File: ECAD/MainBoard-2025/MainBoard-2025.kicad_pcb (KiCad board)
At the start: 2 copper layers, 56 x 151 mm, 144 parts, among them J1 XT60, J12 Conn_01x04, J15 Conn_01x02, J16 XT30, J18 Conn_01x02, J2 Conn_01x04, J20 BAU, J21 BAU, J22 Conn_01x04, J23 Conn_01x02, J26 BAU, J28 Conn_01x02, J4 Conn_01x02, J6 Conn_01x06, J7 XT30, J8 Conn_01x02, J9 Conn_01x02, K2 FINDER-36.11, U2 R-78B3.3-2.0, U3 R-78B12-2.0, U4 R-78B5.0-2.0, U5 Teensy4.1

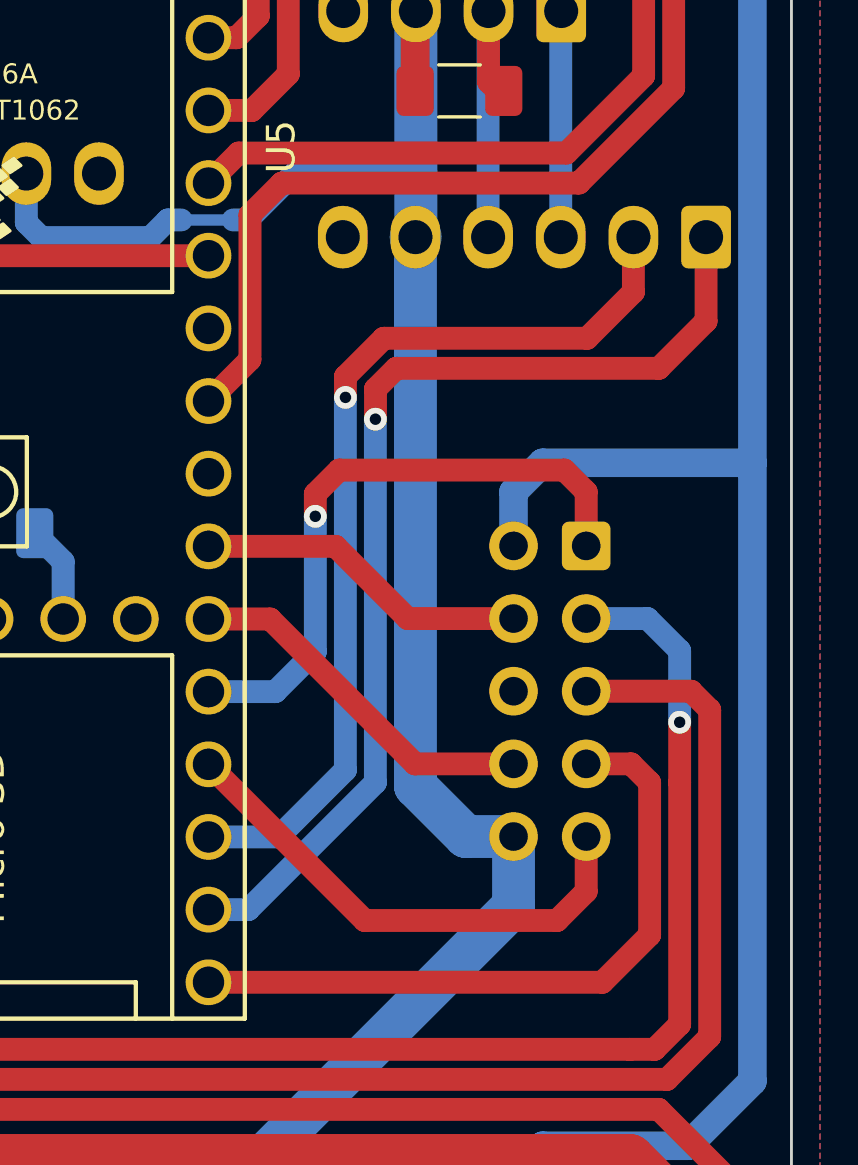
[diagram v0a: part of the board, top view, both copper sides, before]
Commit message: WIP - comatibility 3.x 4.x
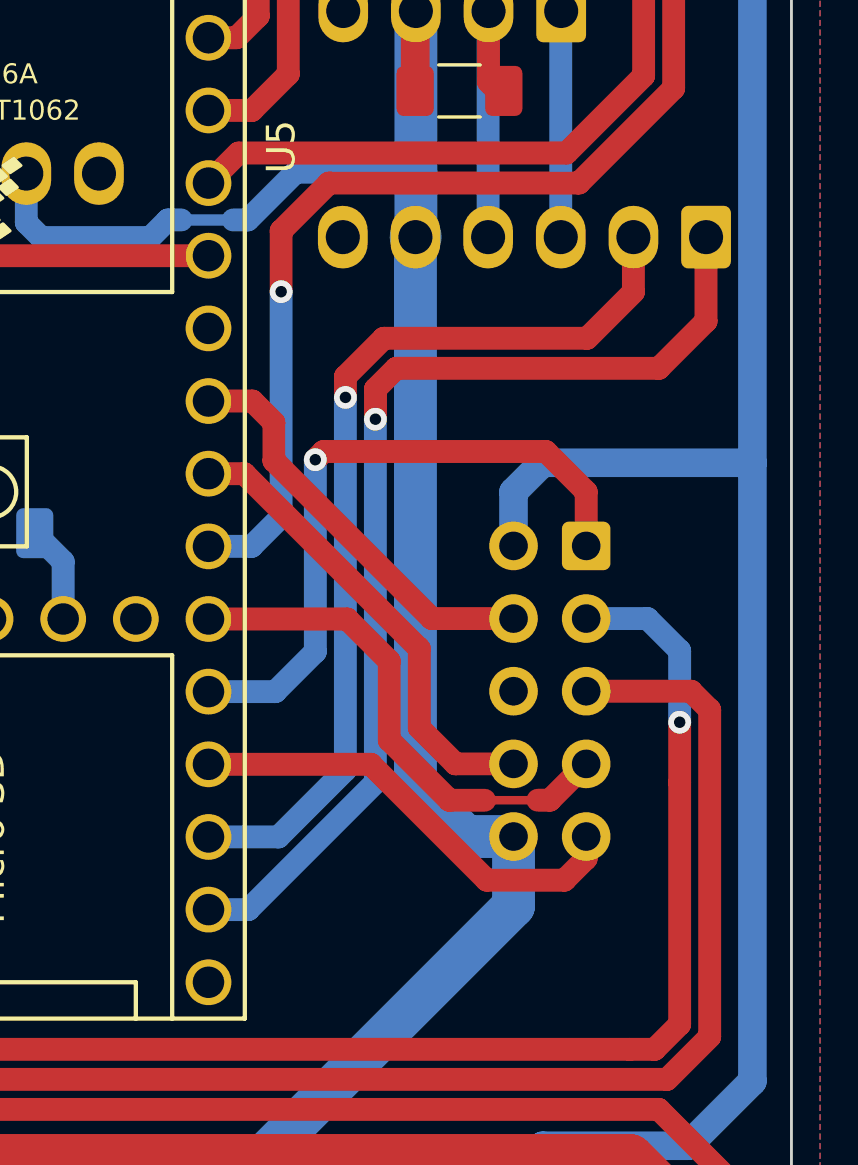
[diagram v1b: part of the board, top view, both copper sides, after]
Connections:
- IHM-IO1 pad 5: Detection -> Tirette-2
- IHM-IO1 pad 7: IHM_3 -> Init-2
- IHM-IO1 pad 9: IHM_4 -> Detection
- U5 pad 24: Detection -> Tirette-2
- U5 pad 25: IHM_3 -> unconnected-(U5-33_MCLK2-Pad25)
- U5 pad 28: IHM_4 -> Detection
- U5 pad 30: Analog0 -> Init-2
- U5 pad 31: Analog1 -> C_Act1-6
- U5 pad 32: unconnected-(U5-40_A16-Pad32) -> Analog0
- U5 pad 33: C_Act1-6 -> Analog1
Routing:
- net Tirette-2: track 0.00 -> 50.8 mm
- net Detection: track 50.8 -> 16.0 mm
- net IHM_3: track 23.9 -> 0.00 mm
- net Init-2: track 0.00 -> 18.0 mm
- net IHM_4: track 17.8 -> 0.00 mm
- net C_Act1-6: track 45.0 -> 50.0 mm, vias 0 -> 1
- net Analog0: track 12.8 -> 16.5 mm
- net Analog1: track 11.7 -> 14.6 mm
- net NEO_PIXEL: track 21.9 -> 23.1 mm

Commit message: Mise en concordance du buzzer avec carte Pami
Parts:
- removed BZ1: Buzzer, Buzzer_Beeper:Buzzer_15x7.5RM7.6
- added BZ2: Buzzer, Buzzer_Beeper:Buzzer_12x9.5RM7.6, F.Cu at (79.6, 99.0)
- moved G*** 188.9 mm to (-37.9, 192.8)
- moved G*** 188.9 mm to (35.5, 116.3)
- moved G*** 188.9 mm to (2.24, 172.7)
- moved G*** 188.9 mm to (15.2, 137.9)
- moved G*** 188.9 mm to (-47.5, 194.7)
- moved G*** 188.9 mm to (44.9, 116.3)
- moved G*** 188.9 mm to (17.2, 109.0)
- moved G*** 188.9 mm to (-21.2, 199.9)
- moved G*** 188.9 mm to (-16.1, 203.7)
- moved G*** 188.9 mm to (43.6, 193.8)
- moved G*** 188.9 mm to (20.6, 190.1)
- moved G*** 188.9 mm to (-47.8, 179.4)
- moved G*** 188.9 mm to (7.82, 137.9)
- moved kibuzzard-64933096 188.9 mm to (25.3, 191.3)
- moved kibuzzard-6493EE56 188.9 mm to (-30.4, 142.5)
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
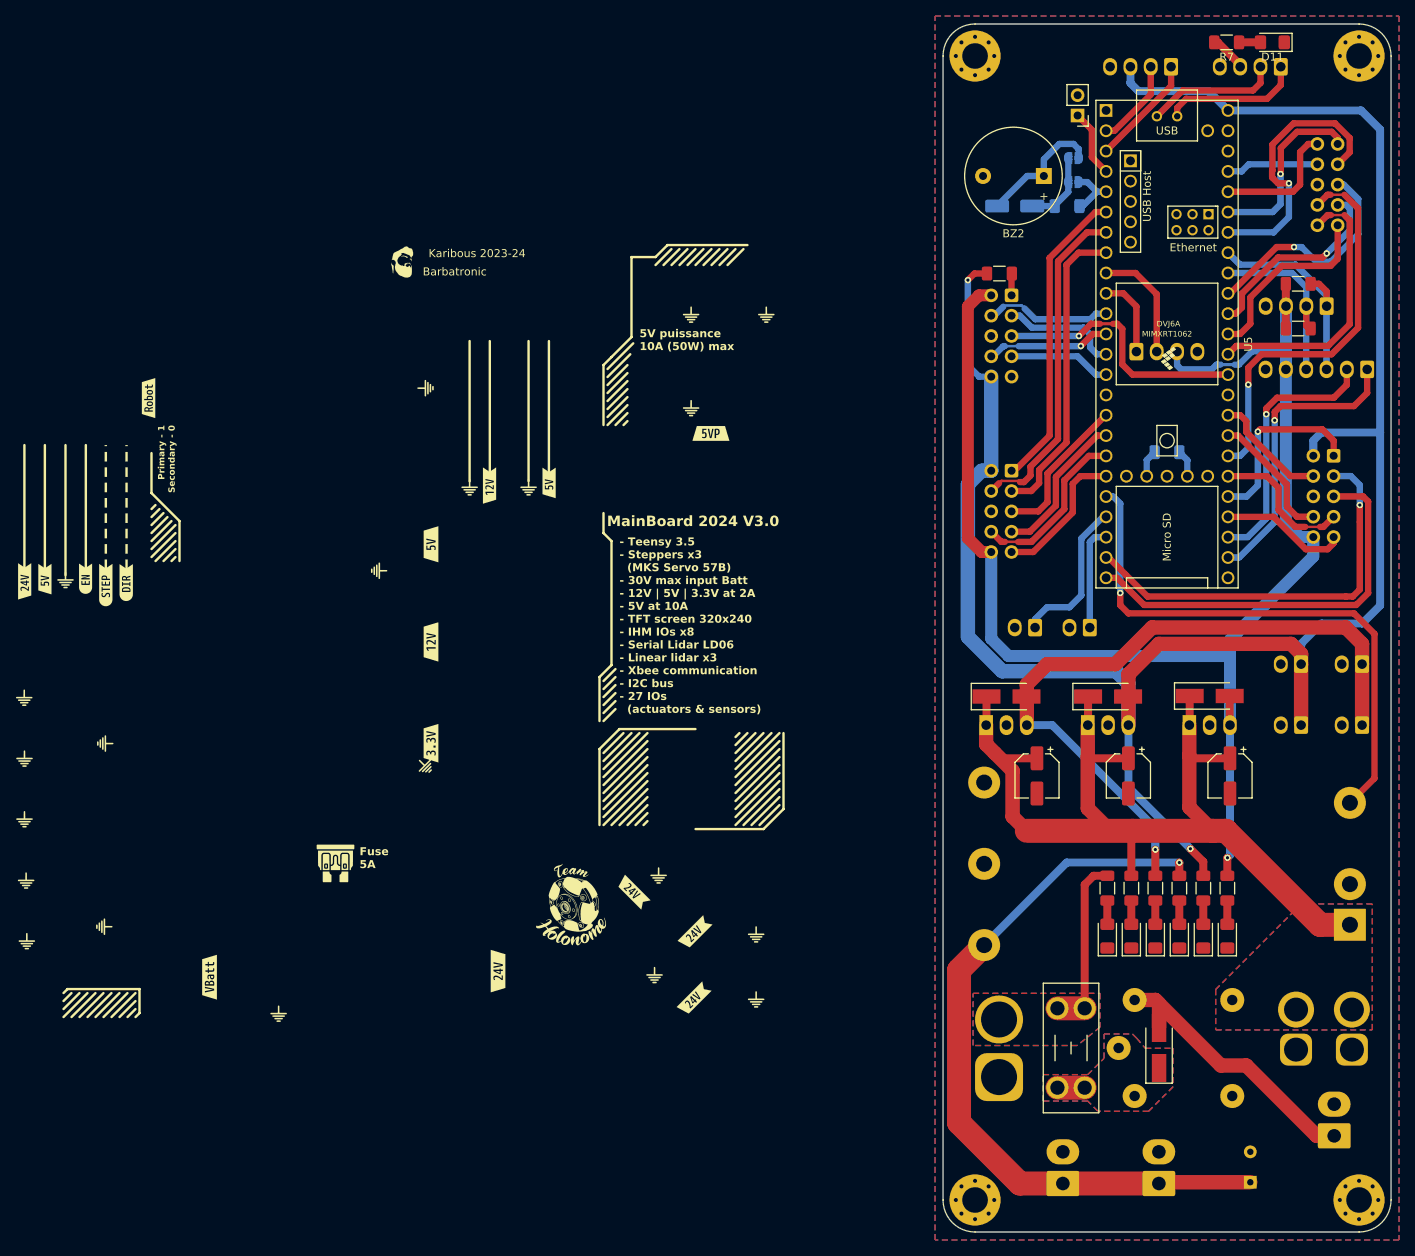
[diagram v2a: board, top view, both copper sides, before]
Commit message: Ne Silkscreen - Optimize for 3.5 and 4.1
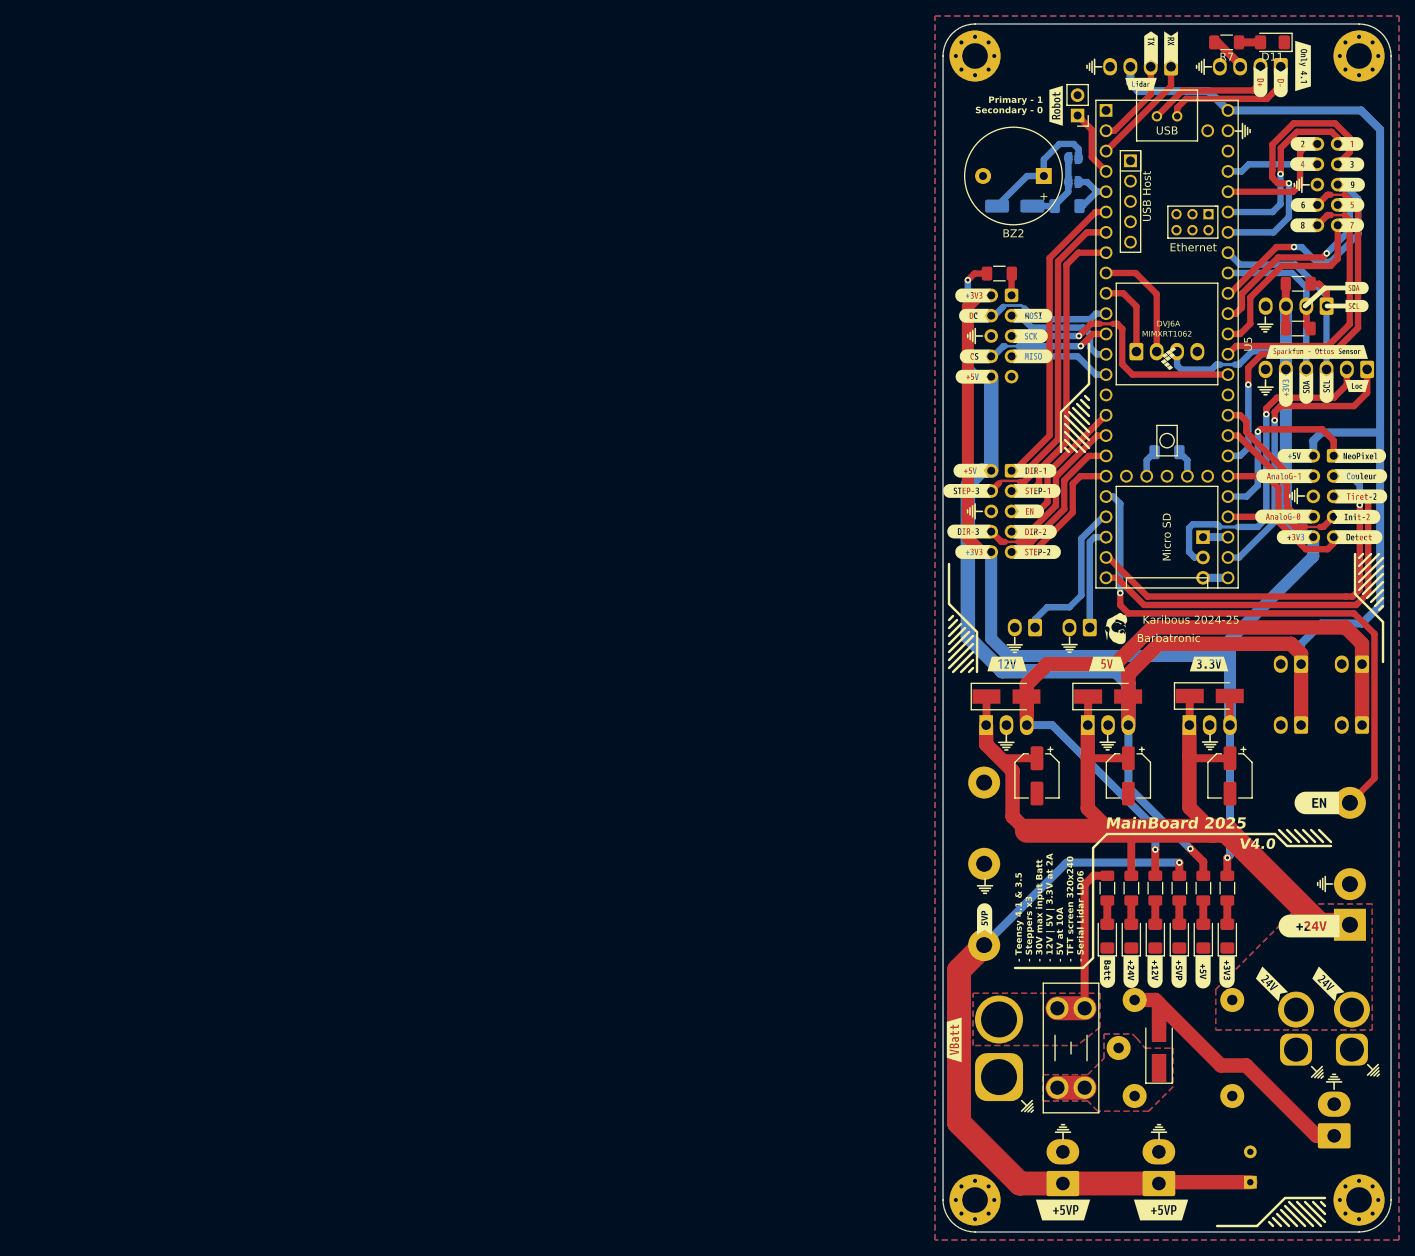
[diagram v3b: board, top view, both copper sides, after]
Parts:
- removed the G*** at (43.6, 201.9)
- removed the G*** at (-3.49, 148.3)
- removed the G*** at (-37.9, 192.8)
- removed the G*** at (35.5, 116.3)
- removed the G*** at (2.24, 172.7)
- removed the G*** at (-42.7, 149.5)
- removed the G*** at (15.2, 137.9)
- removed the G*** at (-47.5, 194.7)
- removed the G*** at (35.5, 128.0)
- removed the G*** at (-47.6, 187.1)
- removed the G*** at (-47.8, 164.2)
- removed the G*** at (31.4, 186.5)
- removed the G*** at (-47.8, 171.8)
- removed the G*** at (44.9, 116.3)
- removed the G*** at (30.9, 198.9)
- removed the G*** at (2.32, 125.5)
- removed the G*** at (-37.7, 169.9)
- removed the G*** at (-30.9, 118.7)
- removed the G*** at (15.2, 115.6)
- removed the G*** at (17.2, 109.0)
- removed the G*** at (7.75, 115.6)
- removed the G*** at (-21.2, 199.9)
- removed the G*** at (-16.1, 203.7)
- removed the G*** at (-42.7, 114.8)
- removed the G*** at (-31.6, 154.7)
- removed the G*** at (30.9, 199.7)
- removed the G*** at (18.7, 181.1)
- removed the G*** at (38.0, 125.2)
- removed the G*** at (43.6, 193.8)
- removed the G*** at (-0.64, 109.7)
- removed the G*** at (-47.8, 179.4)
- removed the G*** at (7.82, 137.9)
- removed the G*** at (-8.94, 184.9)
- removed kibuzzard-64932E55: G***, kibuzzard-64932E55
- removed kibuzzard-64932EB2 (x2): G***, kibuzzard-64932EB2
- removed kibuzzard-64932F6F (x2): G***, kibuzzard-64932F6F
- removed kibuzzard-64933096: G***, kibuzzard-64933096
- removed kibuzzard-64933122: G***, kibuzzard-64933122
- removed kibuzzard-64933136: G***, kibuzzard-64933136
- removed kibuzzard-64933140: G***, kibuzzard-64933140
- removed kibuzzard-6493EE40: G***, kibuzzard-6493EE40
- removed kibuzzard-6493EE50: G***, kibuzzard-6493EE50
- removed kibuzzard-6493EE56: G***, kibuzzard-6493EE56
- removed kibuzzard-6493EE83: G***, kibuzzard-6493EE83
- removed kibuzzard-6493EEE0: G***, kibuzzard-6493EEE0
- removed kibuzzard-6493EEF0: G***, kibuzzard-6493EEF0
- removed kibuzzard-6493EF75: G***, kibuzzard-6493EF75
- removed kibuzzard-6493EFD0: G***, kibuzzard-6493EFD0
- removed kibuzzard-6493EFE7: G***, kibuzzard-6493EFE7
- removed kibuzzard-6493EFEC: G***, kibuzzard-6493EFEC
- removed kibuzzard-6493F0C8: G***, kibuzzard-6493F0C8
- removed kibuzzard-6493F174: G***, kibuzzard-6493F174
- removed kibuzzard-6493F18B: G***, kibuzzard-6493F18B
- removed kibuzzard-6493F190: G***, kibuzzard-6493F190
- removed kibuzzard-649443C2: G***, kibuzzard-649443C2
- removed kibuzzard-649443F6: G***, kibuzzard-649443F6
- removed kibuzzard-64944CDF: G***, kibuzzard-64944CDF
- removed kibuzzard-64944CEA: G***, kibuzzard-64944CEA
- removed kibuzzard-64944CF9: G***, kibuzzard-64944CF9
- removed kibuzzard-64944D19 (x2): G***, kibuzzard-64944D19
- removed the kibuzzard-64944D37 at (35.9, 201.9)
- removed the kibuzzard-64944D37 at (28.3, 188.5)
- removed the kibuzzard-64944D37 at (-47.8, 149.7)
- removed the kibuzzard-64944D37 at (36.0, 193.6)
- removed kibuzzard-64944DAA: G***, kibuzzard-64944DAA
- added G***: LOGO, LOGO, F.Cu at (76.0, 157.6)
- added G***: LOGO, LOGO, F.Cu at (74.9, 169.8)
- added G***: LOGO, LOGO, F.Cu at (82.0, 218.5)
- added G***: LOGO, LOGO, F.Cu at (99.6, 85.4)
- added G***: LOGO, LOGO, F.Cu at (71.0, 119.0)
- added G***: LOGO, LOGO, F.Cu at (82.8, 157.6)
- added G***: LOGO, LOGO, F.Cu at (85.9, 85.4)
- added G***: LOGO, LOGO, F.Cu at (114.8, 187.5)
- added G***: LOGO, LOGO, F.Cu at (111.8, 100.1)
- added G***: LOGO, LOGO, F.Cu at (87.6, 169.8)
- added G***: LOGO, LOGO, F.Cu at (120.8, 210.8)
- added G***: LOGO, LOGO, F.Cu at (113.8, 211.0)
- added G***: LOGO, LOGO, F.Cu at (77.5, 215.2)
- added G***: LOGO, LOGO, F.Cu at (72.2, 187.8)
- added G***: LOGO, LOGO, F.Cu at (94.0, 218.5)
- added G***: LOGO, LOGO, F.Cu at (107.3, 117.6)
- added G***: LOGO, LOGO, B.Cu at (82.5, 85.2)
- added G***: LOGO, LOGO, B.Cu at (81.5, 88.9)
- added G***: LOGO, LOGO, B.Cu at (114.8, 187.5)
- added G***: LOGO, LOGO, B.Cu at (75.4, 185.0)
- added G***: LOGO, LOGO, B.Cu at (83.0, 208.0)
- added G***: LOGO, LOGO, F.Cu at (111.2, 139.0)
- added G***: LOGO, LOGO, B.Cu at (120.8, 210.8)
- added G***: LOGO, LOGO, B.Cu at (115.9, 212.2)
- added G***: LOGO, LOGO, B.Cu at (107.4, 160.0)
- added G***: LOGO, LOGO, B.Cu at (85.9, 85.4)
- added G***: LOGO, LOGO, B.Cu at (82.0, 218.5)
- added G***: LOGO, LOGO, B.Cu at (95.0, 125.5)
- added G***: LOGO, LOGO, B.Cu at (113.8, 211.0)
- added G***: LOGO, LOGO, B.Cu at (77.5, 215.2)
- added G***: LOGO, LOGO, B.Cu at (115.0, 160.0)
- added G***: LOGO, LOGO, B.Cu at (107.4, 167.6)
- added G***: LOGO, LOGO, F.Cu at (104.5, 93.4)
- added G***: LOGO, LOGO, B.Cu at (94.0, 218.5)
- added G***: LOGO, LOGO, B.Cu at (108.7, 214.2)
- added G***: LOGO, LOGO, B.Cu at (115.0, 167.6)
- added G***: LOGO, LOGO, B.Cu at (118.2, 152.8)
- added G***: LOGO, LOGO, F.Cu at (107.3, 125.4)
- added G***: LOGO, LOGO, F.Cu at (115.9, 212.2)
- added G***: LOGO, LOGO, F.Cu at (71.0, 140.9)
- added G***: LOGO, LOGO, F.Cu at (88.6, 155.6)
- added G***: LOGO, LOGO, F.Cu at (100.4, 169.8)
- added J3: Conn_01x03, Connector_PinHeader_2.54mm:PinHeader_1x03_P2.54mm_Vertical, B.Cu at (99.5, 144.1)
- added kibuzzard-64944345: G***, kibuzzard-64944345, B.Cu at (87.5, 160.0)
- added kibuzzard-6494437E: G***, kibuzzard-6494437E, B.Cu at (75.0, 160.0)
- added kibuzzard-64944398: G***, kibuzzard-64944398, B.Cu at (100.2, 160.0)
- added kibuzzard-649443DA: G***, kibuzzard-649443DA, F.Cu at (68.4, 207.0)
- added kibuzzard-64944D37: G***, kibuzzard-64944D37, F.Cu at (115.0, 200.0)
- added kibuzzard-64944D37: G***, kibuzzard-64944D37, F.Cu at (107.9, 200.0)
- added kibuzzard-670C2FEC: G***, kibuzzard-670C2FEC, F.Cu at (93.0, 83.0)
- added kibuzzard-670C2FEC: G***, kibuzzard-670C2FEC, B.Cu at (93.0, 82.2)
- added kibuzzard-670C2FF9: G***, kibuzzard-670C2FF9, F.Cu at (95.5, 83.0)
- added kibuzzard-670C2FF9: G***, kibuzzard-670C2FF9, B.Cu at (95.5, 82.2)
- added kibuzzard-670C3111: G***, kibuzzard-670C3111, B.Cu at (121.0, 100.2)
- added kibuzzard-670C31DA: G***, kibuzzard-670C31DA, F.Cu at (112.8, 192.8)
- added kibuzzard-670C31EF: G***, kibuzzard-670C31EF, F.Cu at (113.7, 177.4)
- added kibuzzard-670C323B: G***, kibuzzard-670C323B, B.Cu at (110.5, 156.0)
- added kibuzzard-670C3244: G***, kibuzzard-670C3244, B.Cu at (118.2, 156.0)
- added kibuzzard-670C3331: G***, kibuzzard-670C3331, F.Cu at (87.6, 198.5)
- added kibuzzard-670C334A: G***, kibuzzard-670C334A, F.Cu at (90.5, 198.5)
- added kibuzzard-670C3352: G***, kibuzzard-670C3352, F.Cu at (93.5, 198.5)
- added kibuzzard-670C3359: G***, kibuzzard-670C3359, F.Cu at (96.5, 198.5)
- added kibuzzard-670C3379: G***, kibuzzard-670C3379, F.Cu at (99.5, 198.5)
- added kibuzzard-670C3380: G***, kibuzzard-670C3380, F.Cu at (102.5, 198.5)
- added kibuzzard-670C33A6: G***, kibuzzard-670C33A6, F.Cu at (94.2, 228.2)
- added kibuzzard-670C33A6: G***, kibuzzard-670C33A6, F.Cu at (82.0, 228.2)
- added kibuzzard-670C33A6: G***, kibuzzard-670C33A6, B.Cu at (82.0, 228.2)
- added kibuzzard-670C33A6: G***, kibuzzard-670C33A6, B.Cu at (94.2, 228.2)
- added kibuzzard-670C3411: G***, kibuzzard-670C3411, B.Cu at (118.1, 199.4)
- added kibuzzard-670C3411: G***, kibuzzard-670C3411, B.Cu at (111.1, 199.4)
- added kibuzzard-670C345D: G***, kibuzzard-670C345D, B.Cu at (80.2, 140.8)
- added kibuzzard-670C34D3: G***, kibuzzard-670C34D3, F.Cu at (70.8, 146.0)
- added kibuzzard-670C34D3: G***, kibuzzard-670C34D3, F.Cu at (111.0, 144.1)
- added kibuzzard-670C34D3: G***, kibuzzard-670C34D3, F.Cu at (109.9, 125.6)
- added kibuzzard-670C34D3: G***, kibuzzard-670C34D3, F.Cu at (70.7, 113.9)
- added kibuzzard-670C34F5: G***, kibuzzard-670C34F5, F.Cu at (111.0, 134.0)
- added kibuzzard-670C34F5: G***, kibuzzard-670C34F5, F.Cu at (70.5, 135.8)
- added kibuzzard-670C34F5: G***, kibuzzard-670C34F5, F.Cu at (70.8, 124.1)
- added kibuzzard-670C3554: G***, kibuzzard-670C3554, F.Cu at (78.5, 135.9)
- added kibuzzard-670C355C: G***, kibuzzard-670C355C, F.Cu at (78.8, 138.4)
- added kibuzzard-670C3560: G***, kibuzzard-670C3560, F.Cu at (77.8, 140.9)
- added kibuzzard-670C3565: G***, kibuzzard-670C3565, F.Cu at (78.5, 143.5)
- added kibuzzard-670C356A: G***, kibuzzard-670C356A, F.Cu at (78.8, 146.0)
- added kibuzzard-670C3571: G***, kibuzzard-670C3571, F.Cu at (70.2, 143.4)
- added kibuzzard-670C3577: G***, kibuzzard-670C3577, F.Cu at (70.0, 138.4)
- added kibuzzard-670C35E1: G***, kibuzzard-670C35E1, F.Cu at (71.0, 121.6)
- added kibuzzard-670C35E9: G***, kibuzzard-670C35E9, F.Cu at (70.9, 116.5)
- added kibuzzard-670C35F6: G***, kibuzzard-670C35F6, F.Cu at (78.2, 116.5)
- added kibuzzard-670C35FE: G***, kibuzzard-670C35FE, F.Cu at (77.9, 119.0)
- added kibuzzard-670C3605: G***, kibuzzard-670C3605, F.Cu at (78.2, 121.5)
- added kibuzzard-670C3646: G***, kibuzzard-670C3646, F.Cu at (112.4, 125.5)
- added kibuzzard-670C364B: G***, kibuzzard-670C364B, F.Cu at (114.9, 125.4)
- added kibuzzard-670C3688: G***, kibuzzard-670C3688, F.Cu at (118.9, 144.1)
- added kibuzzard-670C368F: G***, kibuzzard-670C368F, F.Cu at (118.7, 141.6)
- added kibuzzard-670C36A0: G***, kibuzzard-670C36A0, F.Cu at (119.2, 139.1)
- added kibuzzard-670C36A7: G***, kibuzzard-670C36A7, F.Cu at (119.2, 136.5)
- added kibuzzard-670C36BE: G***, kibuzzard-670C36BE, F.Cu at (119.2, 134.0)
- added kibuzzard-670C36EB: G***, kibuzzard-670C36EB, F.Cu at (109.7, 136.5)
- added kibuzzard-670C36F4: G***, kibuzzard-670C36F4, F.Cu at (109.6, 141.6)
- added kibuzzard-670C375F: G***, kibuzzard-670C375F, B.Cu at (94.9, 131.4)
- added kibuzzard-670C379B: G***, kibuzzard-670C379B, F.Cu at (112.0, 95.0)
- added kibuzzard-670C37A2: G***, kibuzzard-670C37A2, F.Cu at (112.0, 97.5)
- added kibuzzard-670C37B4: G***, kibuzzard-670C37B4, F.Cu at (112.1, 102.6)
- added kibuzzard-670C37B9: G***, kibuzzard-670C37B9, F.Cu at (112.0, 105.2)
- added kibuzzard-670C37C6: G***, kibuzzard-670C37C6, F.Cu at (118.0, 95.0)
- added kibuzzard-670C37D3: G***, kibuzzard-670C37D3, F.Cu at (118.0, 97.5)
- added kibuzzard-670C37D7: G***, kibuzzard-670C37D7, F.Cu at (118.1, 100.1)
- added kibuzzard-670C37DD: G***, kibuzzard-670C37DD, F.Cu at (118.1, 102.6)
- added kibuzzard-670C37E0: G***, kibuzzard-670C37E0, F.Cu at (118.0, 105.2)
- added kibuzzard-670C381F: G***, kibuzzard-670C381F, F.Cu at (106.7, 87.2)
- added kibuzzard-670C3826: G***, kibuzzard-670C3826, F.Cu at (109.2, 87.3)
- added kibuzzard-670C3843: G***, kibuzzard-670C3843, F.Cu at (112.0, 85.2)
- added kibuzzard-670C3846: G***, kibuzzard-670C3846, B.Cu at (112.0, 85.2)
- added kibuzzard-670C3872: G***, kibuzzard-670C3872, F.Cu at (91.8, 87.5)
- added kibuzzard-670C3891: G***, kibuzzard-670C3891, F.Cu at (118.8, 125.2)
- added kibuzzard-670C3891: G***, kibuzzard-670C3891, B.Cu at (119.0, 127.0)
- added kibuzzard-670C38D3: G***, kibuzzard-670C38D3, F.Cu at (113.8, 121.0)
- added kibuzzard-670C38FC: G***, kibuzzard-670C38FC, F.Cu at (118.8, 113.0)
- added kibuzzard-670C3904: G***, kibuzzard-670C3904, F.Cu at (118.8, 115.2)
- added kibuzzard-670C3A1A: G***, kibuzzard-670C3A1A, F.Cu at (72.2, 191.9)
- added kibuzzard-670C3EA9: G***, kibuzzard-670C3EA9, B.Cu at (96.5, 144.1)
- added kibuzzard-670C3EB4: G***, kibuzzard-670C3EB4, B.Cu at (96.5, 149.2)
- added kibuzzard-670C3F16: G***, kibuzzard-670C3F16, B.Cu at (95.0, 117.0)
- G***, kibuzzard-649443DA: moved to B.Cu
- moved kibuzzard-6493EE9E 163.4 mm to (117.5, 115.2), turned to 90 degrees
- moved kibuzzard-6493F100 152.4 mm to (120.2, 139.2)
- moved G*** 137.4 mm to (146.2, 134.8), turned to 180 degrees
- moved kibuzzard-6493F09E 135.9 mm to (88.0, 155.5)
- moved kibuzzard-6493EEAC 135.3 mm to (84.5, 83.0)
- moved kibuzzard-6493F0E7 131.9 mm to (80.0, 119.2)
- moved kibuzzard-6493F0A8 120.0 mm to (73.5, 155.5), turned to -90 degrees
- moved kibuzzard-6494443F 119.2 mm to (81.1, 90.2)
- moved kibuzzard-64944398 97.8 mm to (100.2, 160.0), turned to 0 degrees
- moved kibuzzard-649443DA 93.4 mm to (68.4, 207.0), turned to -90 degrees
- moved kibuzzard-64944345 85.8 mm to (87.5, 160.0), turned to 0 degrees
- moved kibuzzard-6494437E 72.1 mm to (75.0, 160.0), turned to 0 degrees
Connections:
- U5 pad 25: unconnected-(U5-33_MCLK2-Pad25) -> Net-(J3-Pin_3)
- U5 pad 27: RX-loc -> Net-(J3-Pin_1)
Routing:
- net RX-loc: track 32.7 -> 42.4 mm
- net Net-(J3-Pin_3): track 0.00 -> 3.12 mm
- net Net-(J3-Pin_1): track 0.00 -> 3.12 mm
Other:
- board text added: "- Teensy 4.1 & 3.5 - Steppers x3 - 30V max input Batt - 12V | 5V | 3.3V at 2A - 5V at 10A - TFT screen 320x240 - Serial Lidar LD06"
- board text added: "Karibous 2024-25"
- board text added: "MainBoard 2025"
- board text added: "V4.0"
- board text removed: "- Teensy 3.5 - Steppers x3 (MKS Servo 57B) - 30V max input Batt - 12V | 5V | 3.3V at 2A - 5V at 10A - TFT screen 320x240 - IHM IOs x8 - Serial Lidar LD06 - Linear lidar x3 - Xbee communication - I2C bus - 27 IOs (actuators & sensors)"
- board text removed: "Fuse 5A"
- board text removed: "Karibous 2023-24"
- board text removed: "MainBoard 2024 V3.0"
